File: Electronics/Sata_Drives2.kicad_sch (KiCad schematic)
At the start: 66 parts

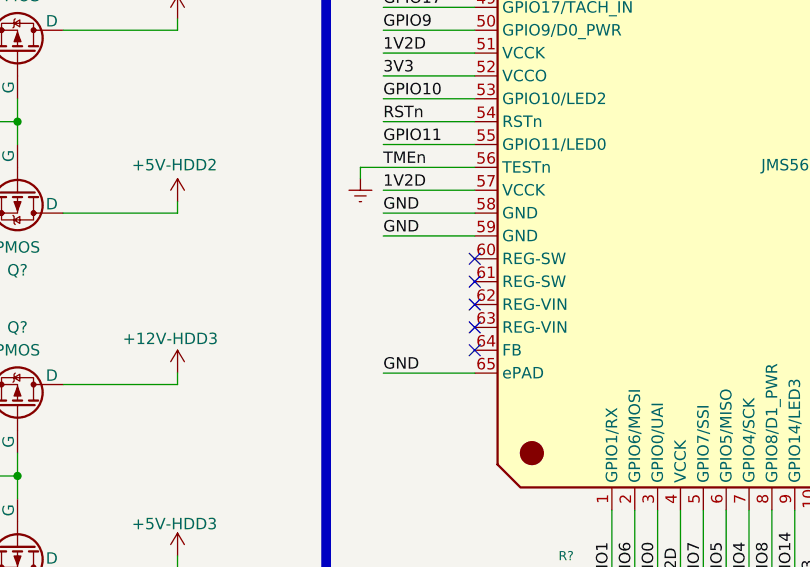
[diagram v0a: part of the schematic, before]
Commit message: RP2040 Added, Files Structure Changed
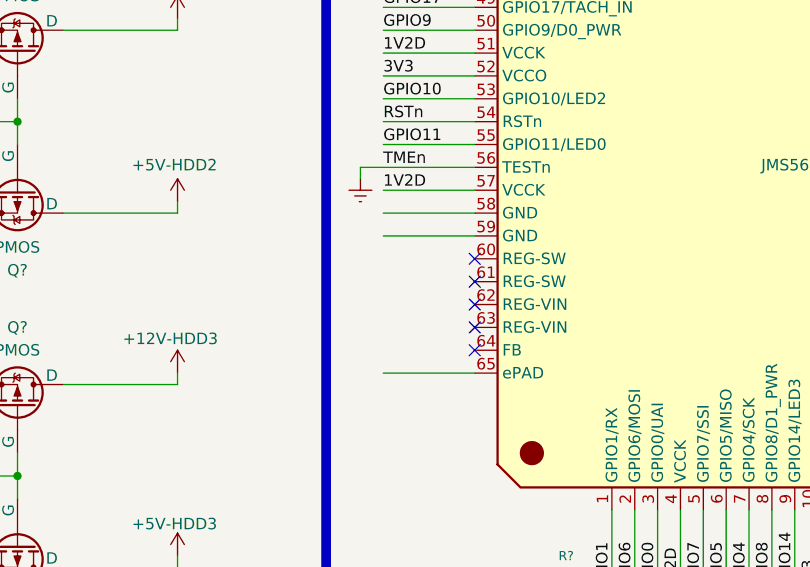
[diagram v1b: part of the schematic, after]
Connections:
- net GND: no longer names the net of U?.58 (GND), U?.59 (GND), U?.65 (ePAD)
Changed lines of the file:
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@@
 		)
 	)
-	(label "GND"
+	(label ""
 		(at 113.03 72.39 0)
 		(effects
@@
 		)
 	)
-	(label "GND"
+	(label ""
 		(at 113.03 74.93 0)
 		(effects
@@
 		)
 	)
-	(label "GND"
+	(label ""
 		(at 113.03 90.17 0)
 		(effects

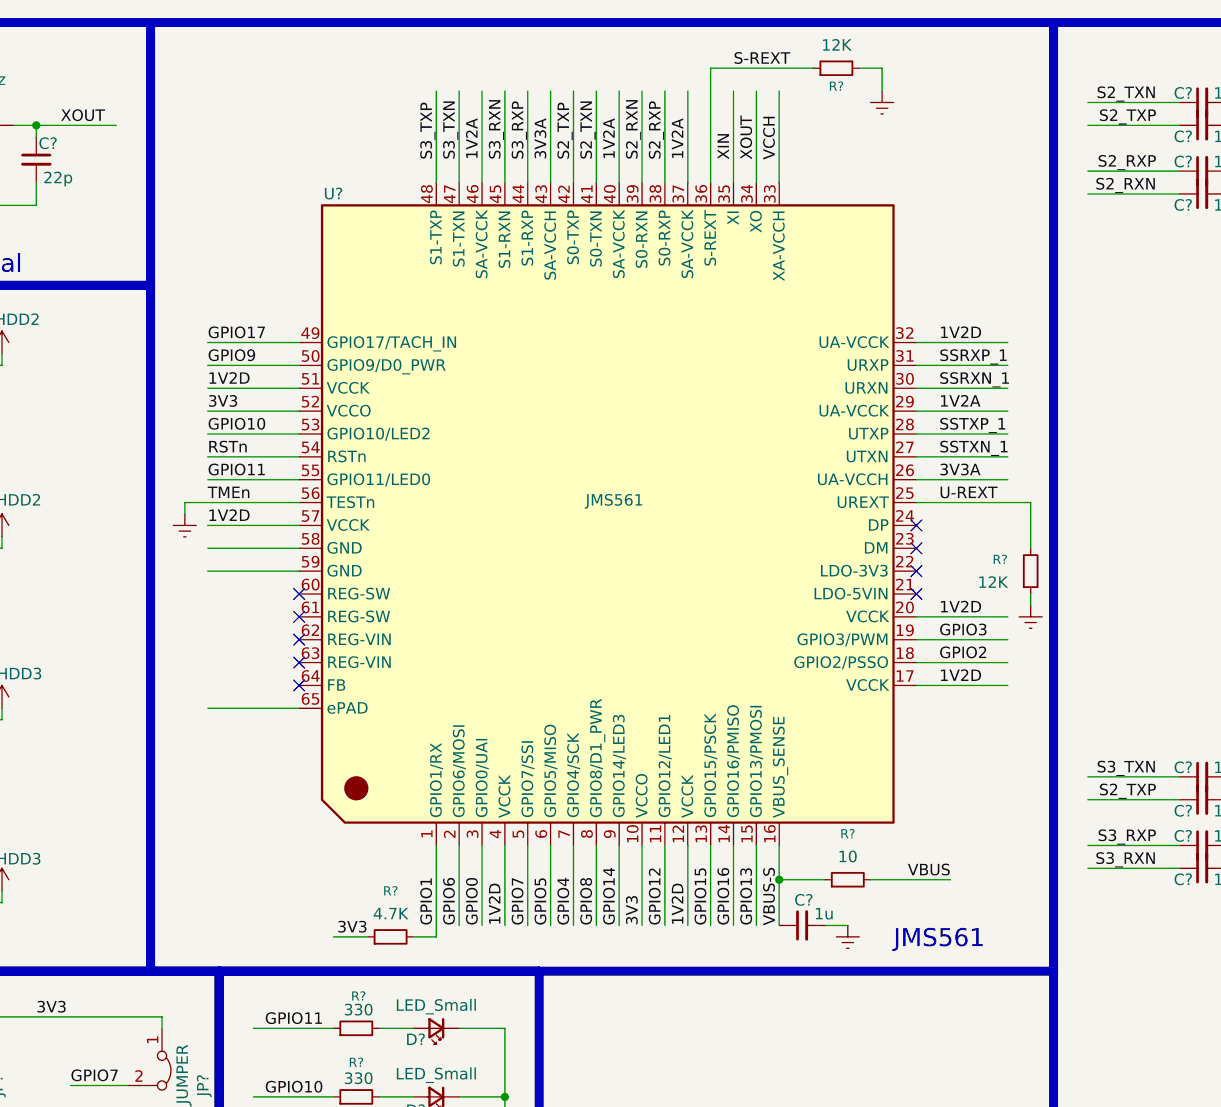
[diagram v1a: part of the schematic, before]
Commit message: Rp2040 Power Sequence finished and general cleaning
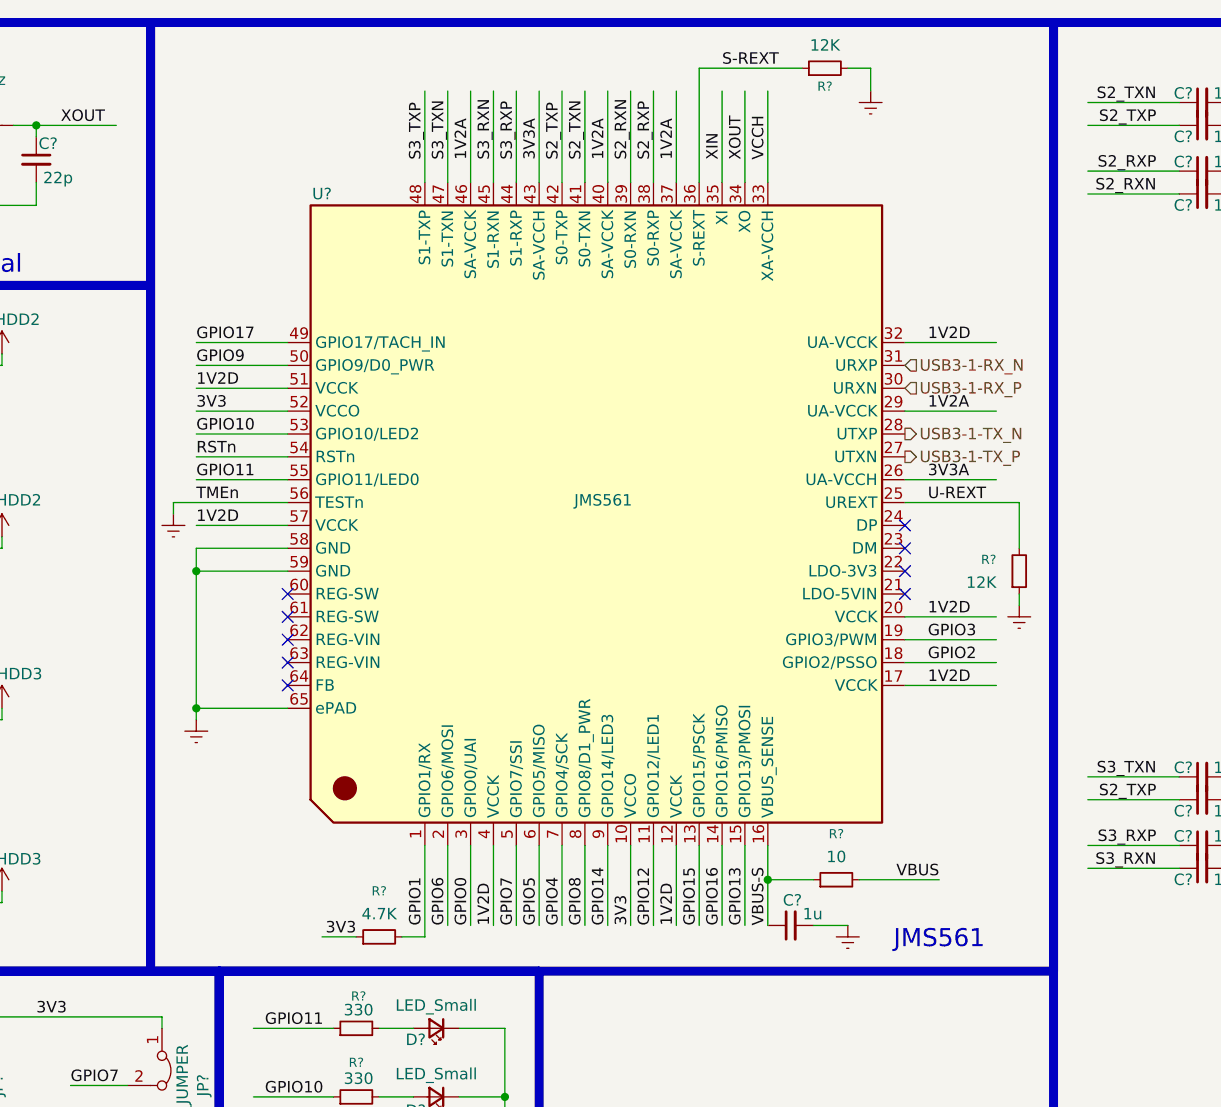
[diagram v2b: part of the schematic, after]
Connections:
- net SSRXN_1 renamed USB3-1-RX_P
- net SSRXP_1 renamed USB3-1-RX_N
- net SSTXN_1 renamed USB3-1-TX_P
- net SSTXP_1 renamed USB3-1-TX_N
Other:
- moved on the sheet: C?, R?, U?

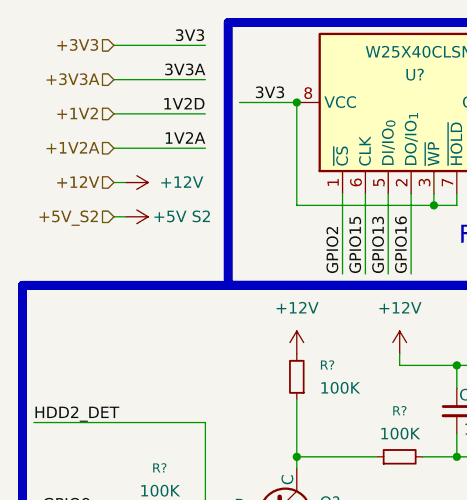
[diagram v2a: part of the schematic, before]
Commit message: Starting the Sheet connections
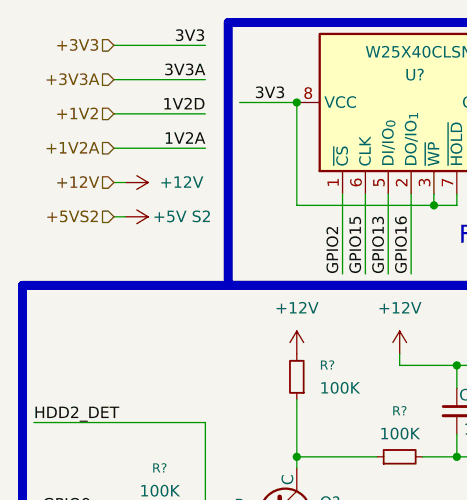
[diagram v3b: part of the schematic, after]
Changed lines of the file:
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@@
 		)
 	)
-	(hierarchical_label "+5V_S2"
+	(hierarchical_label "+5VS2"
 		(shape input)
 		(at 22.86 35.56 180)

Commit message: Footprints Selected
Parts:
- removed C? (x2): 22p, symbol Device:C_Small
- removed D? (x4): LED_Small, symbol Device:LED_Small
- removed R? (x4): 330, symbol Device:R_Small
- removed Y?: 30MHz, symbol Device:Crystal
- added C132, C133: 22p, Capacitor_SMD:C_0603_1608Metric, symbol Device:C_Small
- added D20, D21, D22, D23: LED Green, LED_SMD:LED_0603_1608Metric, symbol Device:LED
- added R76, R77, R78, R79: 1k, Resistor_SMD:R_0603_1608Metric, symbol Device:R_Small
- added Y2: 30MHz, ABM8-30.000MHZ-B2-T:ABM810000MHZ12D2W, symbol Device:Crystal_GND24
- C118, C119, C120, C121, C122, C123, C124, C125, C126, C127, C128, C129, C130, C131, C134, C135, C136, C137, C138, C139, C140, C141, C142, C143, C144, C145, C146: renamed from C?; footprint (none) -> Capacitor_SMD:C_0603_1608Metric
- JP4, JP5: renamed from JP?; footprint (none) -> Connector_PinHeader_2.54mm:PinHeader_1x03_P2.54mm_Vertical
- Q12, Q13, Q18, Q19: renamed from Q?; footprint (none) -> MMBT3904:P200_SOT-23
- Q14, Q15, Q16, Q17: renamed from Q?; footprint (none) -> AOSS21311C:SOT95P237X117-3N
- R68, R69, R70, R71, R72, R73, R74, R75, R81, R82, R83, R84, R85: renamed from R?; footprint (none) -> Resistor_SMD:R_0603_1608Metric
- R80: renamed from R?; value 4.7K -> 4.7K 1%; footprint (none) -> Resistor_SMD:R_0603_1608Metric
- gave numbers to parts that had none: 4
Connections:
- net +12V-HDD2: now also C145.1, J22.P13, J22.P14, J22.P15; no longer C144.1, J22.P7, J22.P8, J22.P9
- net +5V-HDD2: now also C144.1, J22.P7, J22.P8, J22.P9; no longer C145.1, J22.P13, J22.P14, J22.P15
- net GPIO10: now also R77.1
- net GPIO11: now also R76.1
- net GPIO12: now also R78.1
- net GPIO14: now also R79.1
- net XIN: now also C132.1, Y2.1
- net XOUT: now also C133.1, Y2.3
- new net: C132.2, C133.2, Y2.4
- new net: D21.2 (A), R77.2
- new net: D20.1 (K), D21.1 (K), D22.1 (K), D23.1 (K)
- new net: D22.2 (A), R78.2
- new net: D20.2 (A), R76.2
- new net: D23.2 (A), R79.2

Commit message: Footprints selected, Hiracicle connections created, Pcb next
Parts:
- C118: renamed from C135; footprint Capacitor_SMD:C_0603_1608Metric -> Capacitor_SMD:C_0402_1005Metric
- C119: renamed from C136; footprint Capacitor_SMD:C_0603_1608Metric -> Capacitor_SMD:C_0402_1005Metric
- C120: renamed from C132; footprint Capacitor_SMD:C_0603_1608Metric -> Capacitor_SMD:C_0402_1005Metric
- C121: renamed from C133; footprint Capacitor_SMD:C_0603_1608Metric -> Capacitor_SMD:C_0402_1005Metric
- C122: renamed from C137; footprint Capacitor_SMD:C_0603_1608Metric -> Capacitor_SMD:C_0402_1005Metric
- C123: renamed from C138; footprint Capacitor_SMD:C_0603_1608Metric -> Capacitor_SMD:C_0402_1005Metric
- C124: renamed from C144; footprint Capacitor_SMD:C_0603_1608Metric -> Capacitor_SMD:C_1206_3216Metric
- C125: renamed from C145; footprint Capacitor_SMD:C_0603_1608Metric -> Capacitor_SMD:C_1206_3216Metric
- C126: renamed from C128; footprint Capacitor_SMD:C_0603_1608Metric -> Capacitor_SMD:C_0805_2012Metric
- C127: renamed from C129; footprint Capacitor_SMD:C_0603_1608Metric -> Capacitor_SMD:C_0805_2012Metric
- C128: renamed from C139; footprint Capacitor_SMD:C_0603_1608Metric -> Capacitor_SMD:C_0402_1005Metric
- C129: renamed from C140; footprint Capacitor_SMD:C_0603_1608Metric -> Capacitor_SMD:C_0402_1005Metric
- C130: renamed from C141; footprint Capacitor_SMD:C_0603_1608Metric -> Capacitor_SMD:C_0402_1005Metric
- C131: renamed from C142; footprint Capacitor_SMD:C_0603_1608Metric -> Capacitor_SMD:C_0402_1005Metric
- C133: renamed from C143; footprint Capacitor_SMD:C_0603_1608Metric -> Capacitor_SMD:C_1206_3216Metric
- C134: renamed from C146; footprint Capacitor_SMD:C_0603_1608Metric -> Capacitor_SMD:C_1206_3216Metric
- C141: renamed from C124; footprint Capacitor_SMD:C_0603_1608Metric -> Capacitor_SMD:C_0805_2012Metric
- C142: renamed from C126; footprint Capacitor_SMD:C_0603_1608Metric -> Capacitor_SMD:C_0805_2012Metric
- C145: renamed from C120; footprint Capacitor_SMD:C_0603_1608Metric -> Capacitor_SMD:C_0805_2012Metric
- R71: renamed from R68; value 4.7K -> 4K7
- R78: renamed from R69; value 4.7K -> 4K7
- R79: renamed from R80; value 4.7K 1% -> 4K7 1%
- R80: renamed from R76; value 1k -> 270
- R81: renamed from R77; value 1k -> 270
- R82: renamed from R78; value 1k -> 270
- R83: renamed from R79; value 1k -> 270
- renumbered C134 to C132, C118 to C135, C121 to C136, C125 to C137, C130 to C138, C119 to C139, C122 to C140, C127 to C143, C131 to C144, C123 to C146, D20 to D18, D21 to D19, D22 to D20, D23 to D21, JP4 to JP3, JP5 to JP4, Q19 to Q10, Q14 to Q11, Q15 to Q13, Q16 to Q14, Q18 to Q15, Q13 to Q16, R81 to R66, R84 to R67, R72 to R68, R74 to R69, R83 to R72, R85 to R74, R71 to R76, R82 to R77
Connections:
- net TMEn is gone; now on net gnd: U12.56 (TESTn)
- net gnd: now reaches Q10.3 (E)
- net gnd: now also C120.2, C121.2, C124.2, C125.2, C132.2, C133.2, C134.2, C135.2, C136.2, C137.2, C138.2, C139.2, C140.2, C141.2, C142.2, C143.2, C144.2, C145.2, C146.2, D18.1 (K), D19.1 (K), D20.1 (K), D21.1 (K), J22.P10, J22.P11, J22.P12, J22.P4, J22.P6, J22.S1, J22.S4, J22.S7, J22.SH1 (SHIELD), J22.SH2 (SHIELD), J23.P10, J23.P11, J23.P12, J23.P4, J23.P6, J23.S1, J23.S4, J23.S7, J23.SH1 (SHIELD), J23.SH2 (SHIELD), JP3.3 (B), JP4.3 (B), Q12.3 (E), Q15.3 (E), Q16.3 (E), R66.2, R71.2, R72.1, R78.2, U11.4 (GND), U12.58 (GND), U12.59 (GND), U12.65 (ePAD), Y2.2, Y2.4

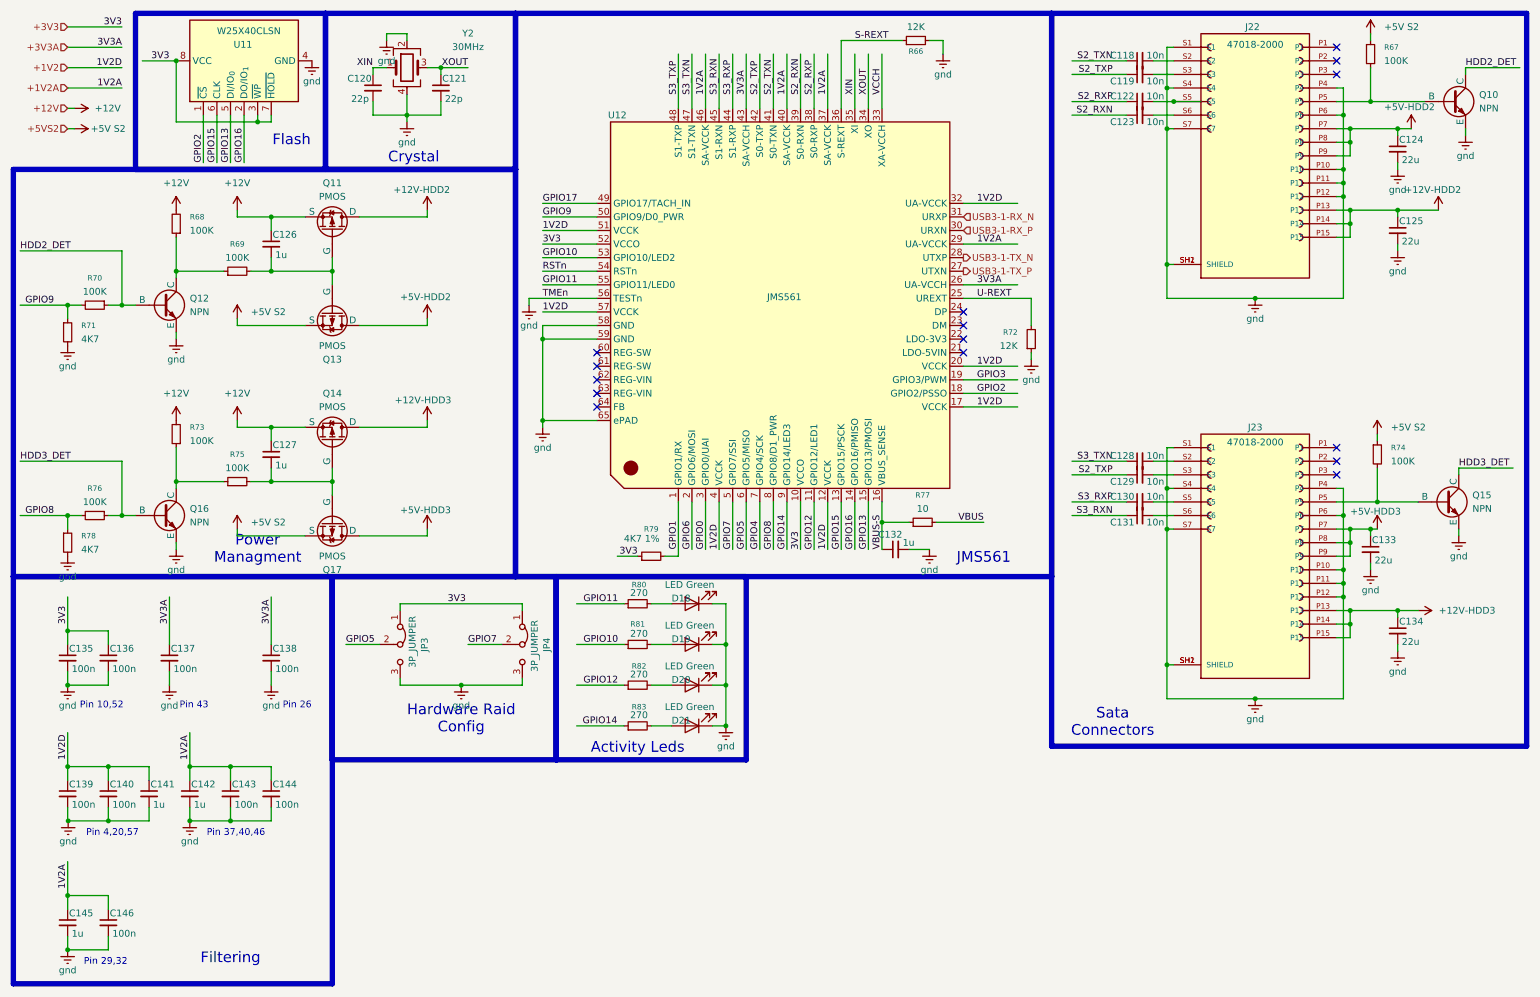
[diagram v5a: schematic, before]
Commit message: Sata Port Changed
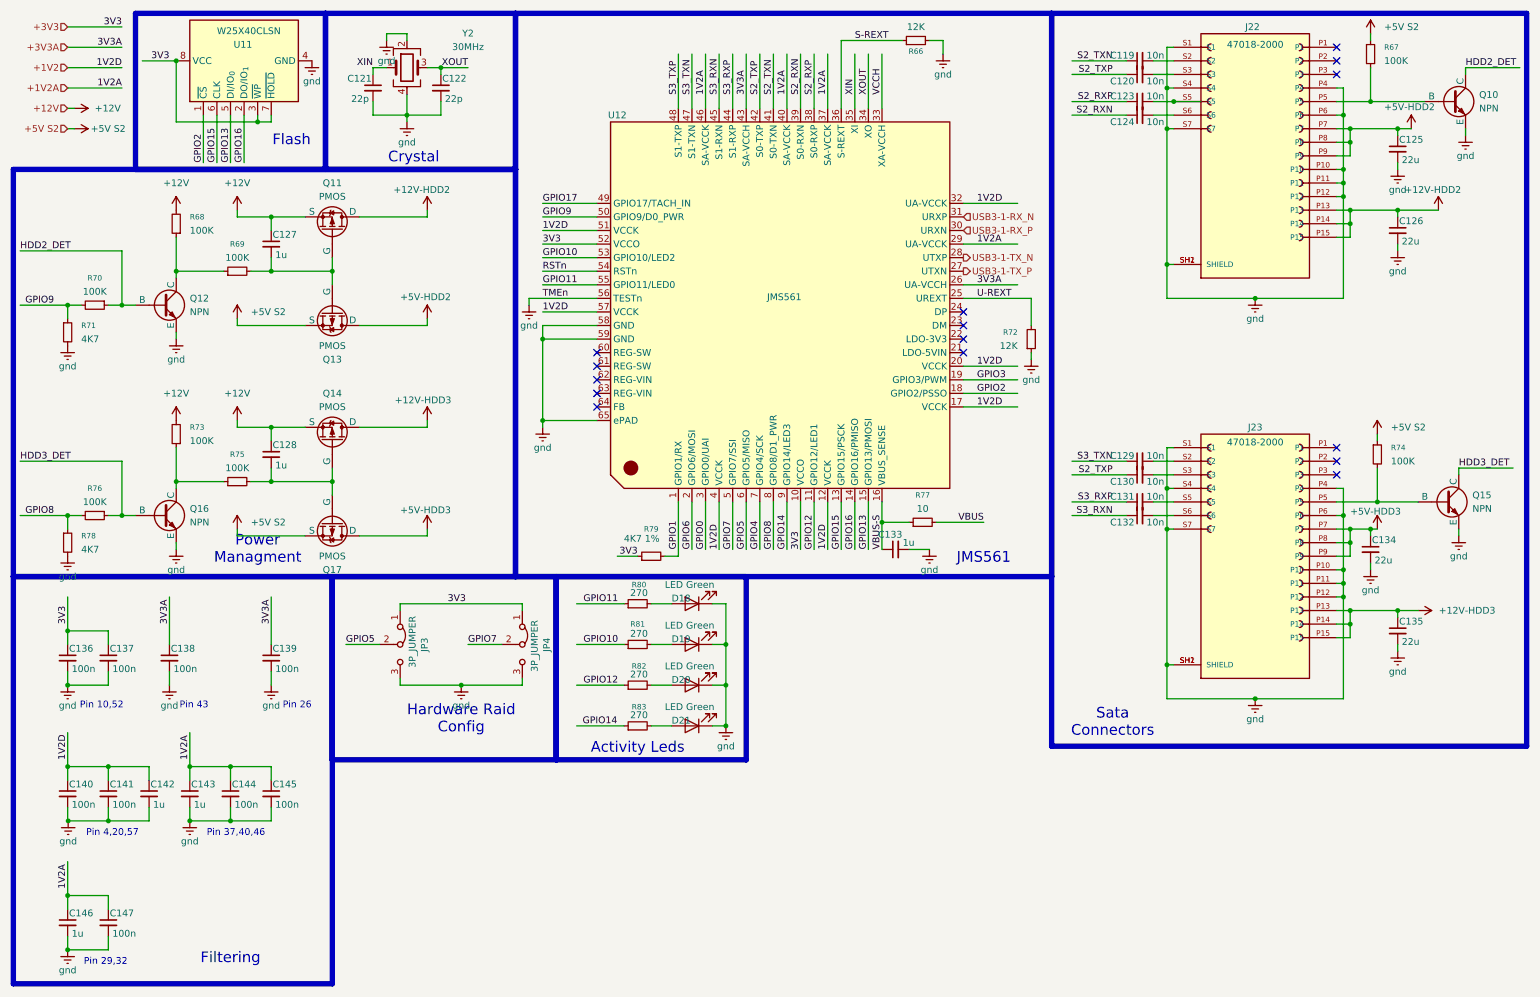
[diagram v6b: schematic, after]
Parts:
- renumbered C118 to C119, C119 to C120, C120 to C121, C121 to C122, C122 to C123, C123 to C124, C124 to C125, C125 to C126, C126 to C127, C127 to C128, C128 to C129, C129 to C130, C130 to C131, C131 to C132, C132 to C133, C133 to C134, C134 to C135, C135 to C136, C136 to C137, C137 to C138, C138 to C139, C139 to C140, C140 to C141, C141 to C142, C142 to C143, C143 to C144, C144 to C145, C145 to C146, C146 to C147
